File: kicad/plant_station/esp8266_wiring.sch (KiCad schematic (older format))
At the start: 20 parts, among them J1 Conn_02x08_Odd_Even, J17 GPIO, J8 UART, Q4 DMG2301L, U4 ESP-WROOM-02, U5 TPL5110

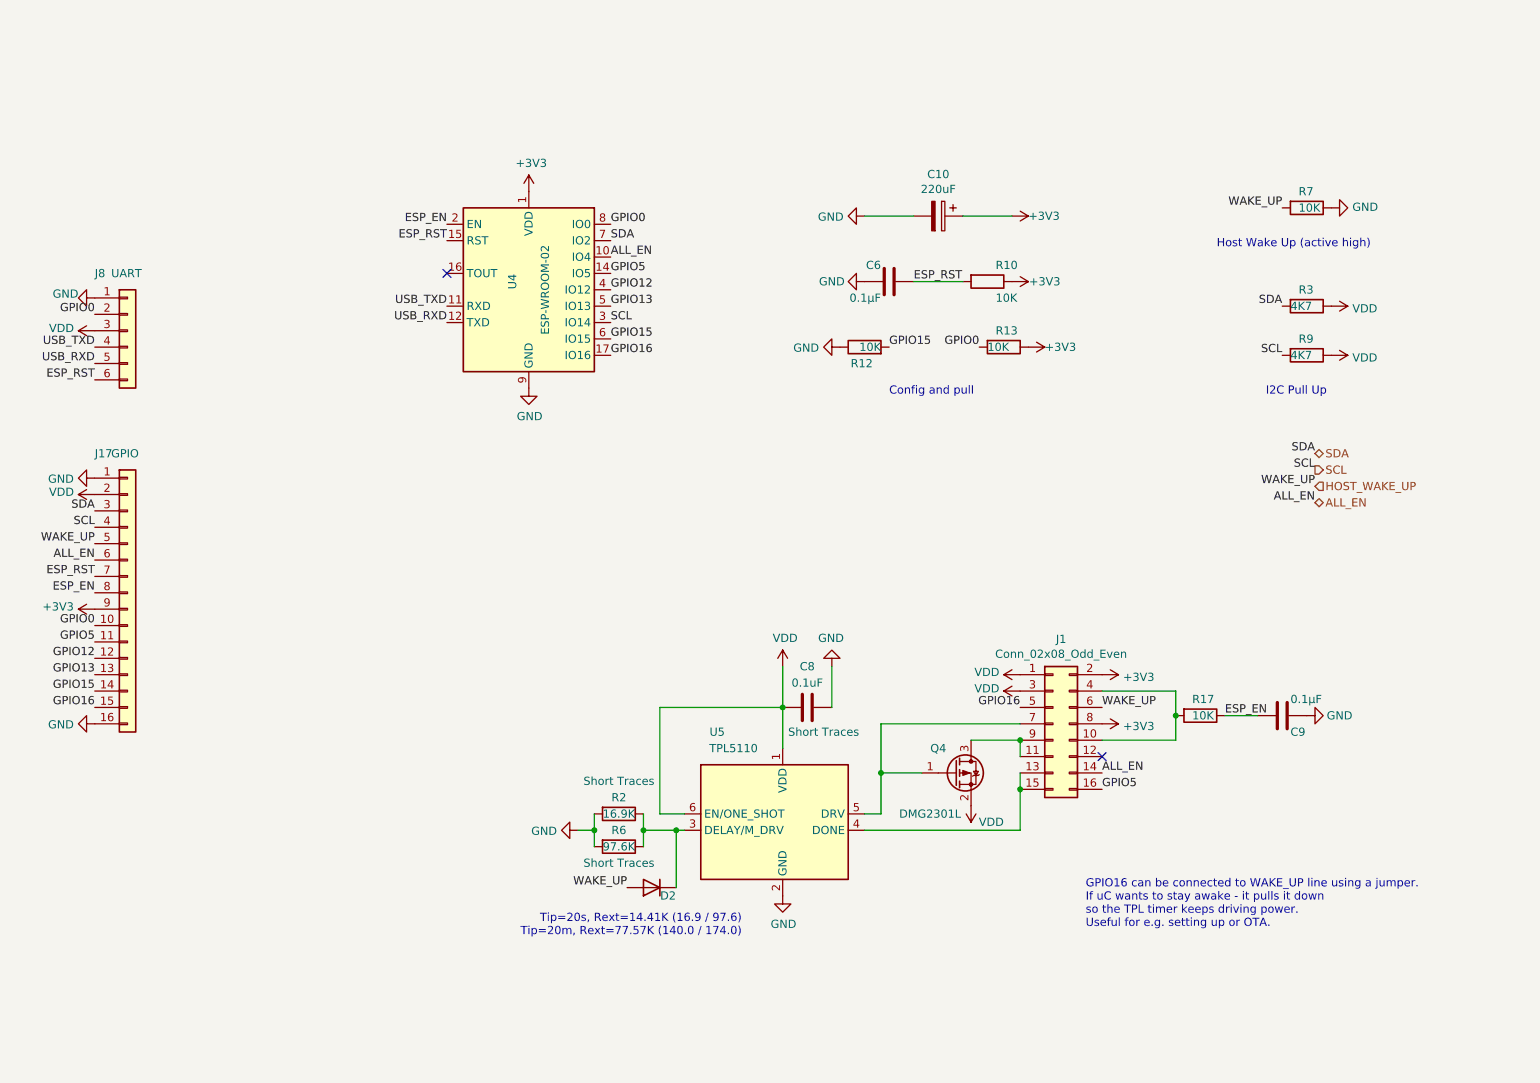
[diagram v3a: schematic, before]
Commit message: Initial board layout complete
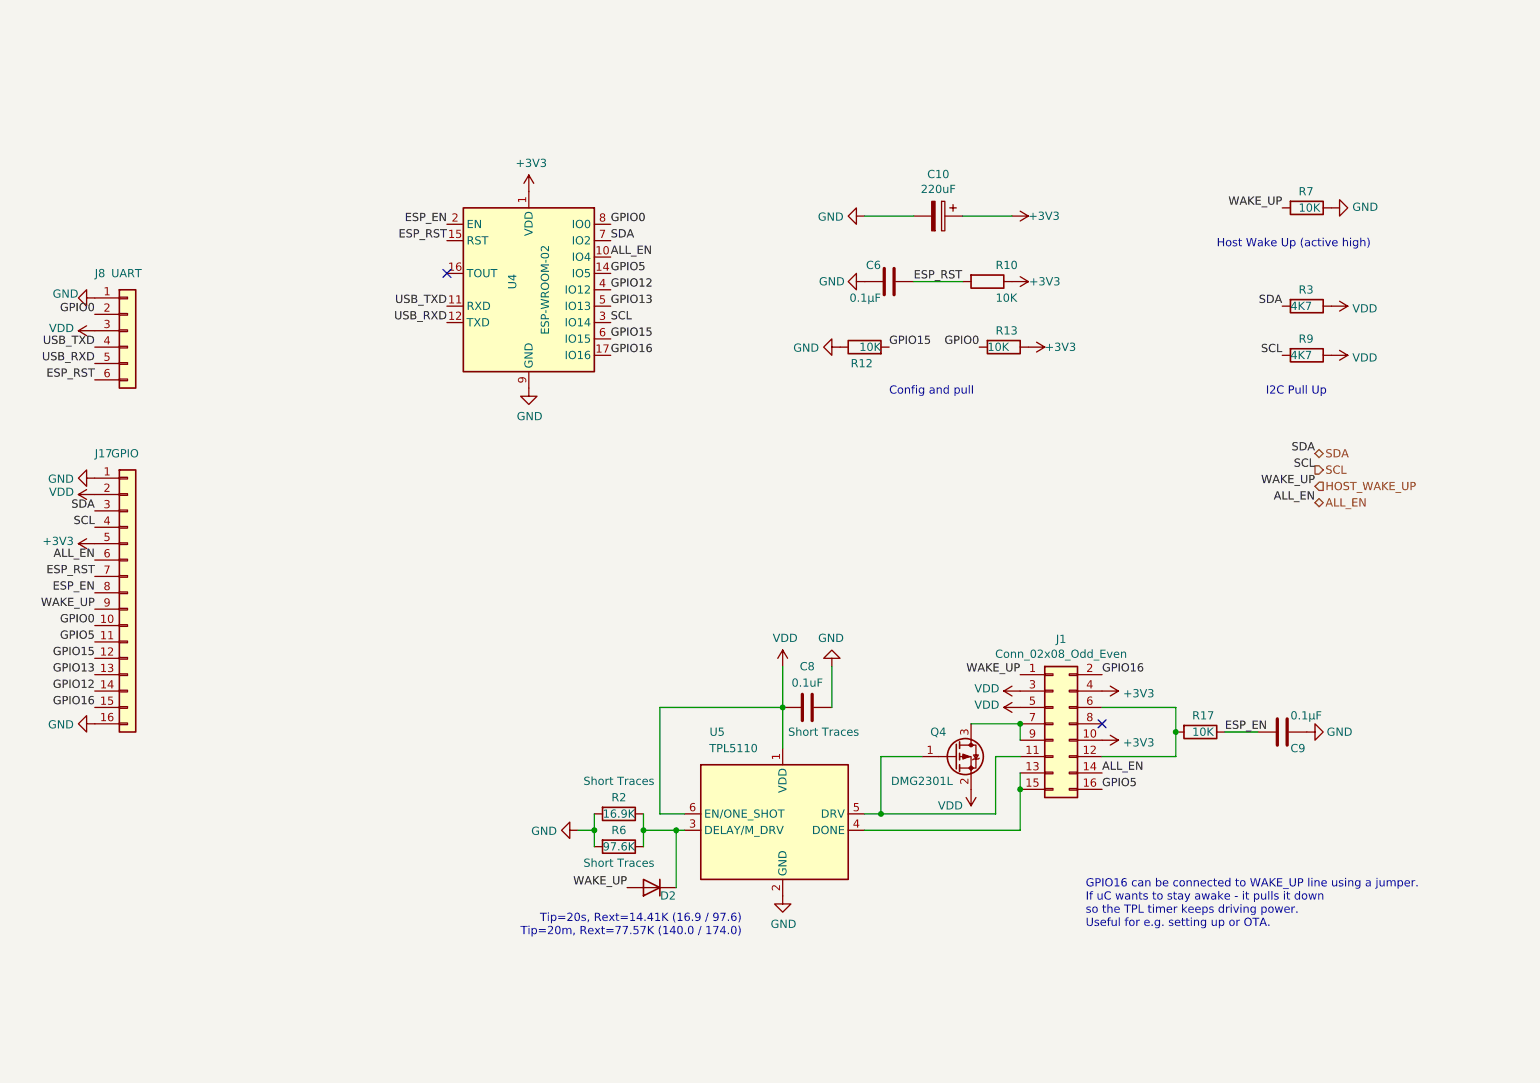
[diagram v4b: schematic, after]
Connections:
- net +3V3: now also J1.10 (Pin_10), J1.4 (Pin_4), J17.5 (Pin_5); no longer J1.2 (Pin_2), J1.8 (Pin_8), J17.9 (Pin_9)
- net GPIO12: now also J17.14 (Pin_14); no longer J17.12 (Pin_12)
- net GPIO15: now also J17.12 (Pin_12); no longer J17.14 (Pin_14)
- net GPIO16: now also J1.2 (Pin_2); no longer J1.5 (Pin_5)
- net HOST_WAKE_UP: now also J1.1 (Pin_1), J17.9 (Pin_9); no longer J1.6 (Pin_6), J17.5 (Pin_5)
- net VDD: now also J1.5 (Pin_5); no longer J1.1 (Pin_1)
- net at Q4.1 (G), U5.5 (DRV): now also J1.11 (Pin_11); no longer J1.7 (Pin_7)
- net at J1.9 (Pin_9), Q4.3 (D): now also J1.7 (Pin_7); no longer J1.11 (Pin_11)
- net at J1.12 (Pin_12): now also J1.6 (Pin_6), R17.2
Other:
- moved on the sheet: C9, Q4, R17
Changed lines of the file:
@@
 	0    1    1    0
 $EndComp
-Text Label 9150 1650 2    50   ~ 0
-WAKE_UP
 Text Notes 8750 1900 0    50   ~ 0
 Host Wake Up (active high)
@@
 	1    0    0    -1
 $EndComp
-Text Label 8050 4700 0    50   ~ 0
+Text Label 7550 4500 2    50   ~ 0
 WAKE_UP
 Text Notes 7950 6050 0    50   ~ 0
@@
 L power:VDD #PWR039
 U 1 1 5F99A85E
-P 7250 5300
-F 0 "#PWR039" H 7250 5150 50  0001 C CNN
-F 1 "VDD" H 7050 5400 50  0000 L CNN
-F 2 "" H 7250 5300 50  0001 C CNN
-F 3 "" H 7250 5300 50  0001 C CNN
-	1    7250 5300
+P 7250 5200
+F 0 "#PWR039" H 7250 5050 50  0001 C CNN
+F 1 "VDD" H 7300 5300 50  0000 L CNN
+F 2 "" H 7250 5200 50  0001 C CNN
+F 3 "" H 7250 5200 50  0001 C CNN
+	1    7250 5200
 	-1   0    0    1
 $EndComp
@@
 L Transistor_FET:DMG2301L Q4
 U 1 1 5F96E6B6
-P 7150 5100
-F 0 "Q4" H 7050 5250 50  0000 C CNN
-F 1 "DMG2301L" H 7000 4850 50  0000 C CNN
-F 2 "Package_TO_SOT_SMD:SOT-23" H 7350 5025 50  0001 L CIN
-F 3 "https://www.diodes.com/assets/Datasheets/DMG2301L.pdf" H 7150 5100 50  0001 L CNN
-	1    7150 5100
-	1    0    0    -1
-$EndComp
-Wire Wire Line
-	6950 5100 6700 5100
-Wire Wire Line
-	6700 5100 6700 5350
+P 7150 5000
+F 0 "Q4" H 7050 5150 50  0000 C CNN
+F 1 "DMG2301L" H 6950 4850 50  0000 C CNN
+F 2 "Package_TO_SOT_SMD:SOT-23" H 7350 4925 50  0001 L CIN
+F 3 "https://www.diodes.com/assets/Datasheets/DMG2301L.pdf" H 7150 5000 50  0001 L CNN
+	1    7150 5000
+	1    0    0    -1
+$EndComp
 Wire Wire Line
 	4950 5450 4850 5450
-Wire Wire Line
-	6700 5100 6700 4800
-Connection ~ 6700 5100
 $Comp
 L power:VDD #PWR033
@@
 Text Label 1900 4300 2    50   ~ 0
 GPIO5
-Text Label 1900 4400 2    50   ~ 0
+Text Label 1900 4600 2    50   ~ 0
 GPIO12
 Text Label 1900 4500 2    50   ~ 0
 GPIO13
-Text Label 1900 4600 2    50   ~ 0
+Text Label 1900 4400 2    50   ~ 0
 GPIO15
-Text Label 1900 3700 2    50   ~ 0
-WAKE_UP
 Text Label 1900 3500 2    50   ~ 0
 SDA
@@
 Text Label 1900 3800 2    50   ~ 0
 ALL_EN
-$Comp
-L power:+3V3 #PWR0104
-U 1 1 5FAF7387
-P 1900 4100
-F 0 "#PWR0104" H 1900 3950 50  0001 C CNN
-F 1 "+3V3" V 1915 4228 50  0000 L CNN
-F 2 "" H 1900 4100 50  0001 C CNN
-F 3 "" H 1900 4100 50  0001 C CNN
-	1    1900 4100
-	0    -1   -1   0
-$EndComp
 Wire Wire Line
 	6700 5350 6600 5350
@@
 $EndComp
 Wire Wire Line
-	9000 4750 8800 4750
-Wire Wire Line
-	8500 4750 8500 4900
-Connection ~ 8500 4750
-Wire Wire Line
-	8050 4900 8500 4900
-Wire Wire Line
-	8500 4600 8500 4750
-Wire Wire Line
-	8050 4600 8500 4600
-NoConn ~ 8050 5000
-Wire Wire Line
-	6700 4800 7550 4800
+	9000 4850 8800 4850
+Wire Wire Line
+	8050 5000 8500 5000
+Wire Wire Line
+	8050 4700 8500 4700
 Wire Wire Line
 	6600 5450 7550 5450
-Wire Wire Line
-	7250 4900 7550 4900
 $Comp
 L power:VDD #PWR040
 U 1 1 5F88FAB9
-P 7550 4500
-F 0 "#PWR040" H 7550 4350 50  0001 C CNN
-F 1 "VDD" V 7565 4627 50  0000 L CNN
-F 2 "" H 7550 4500 50  0001 C CNN
-F 3 "" H 7550 4500 50  0001 C CNN
-	1    7550 4500
-	0    -1   -1   0
-$EndComp
-$Comp
-L power:VDD #PWR041
-U 1 1 5F89065C
 P 7550 4600
-F 0 "#PWR041" H 7550 4450 50  0001 C CNN
+F 0 "#PWR040" H 7550 4450 50  0001 C CNN
 F 1 "VDD" V 7565 4727 50  0000 L CNN
 F 2 "" H 7550 4600 50  0001 C CNN
@@
 	0    -1   -1   0
 $EndComp
-Text Label 8800 4750 0    50   ~ 0
+$Comp
+L power:VDD #PWR041
+U 1 1 5F89065C
+P 7550 4700
+F 0 "#PWR041" H 7550 4550 50  0001 C CNN
+F 1 "VDD" V 7565 4827 50  0000 L CNN
+F 2 "" H 7550 4700 50  0001 C CNN
+F 3 "" H 7550 4700 50  0001 C CNN
+	1    7550 4700
+	0    -1   -1   0
+$EndComp
+Text Label 8800 4850 0    50   ~ 0
 ESP_EN
 $Comp
 L power:+3V3 #PWR043
 U 1 1 5F863AFE
-P 8050 4800
-F 0 "#PWR043" H 8050 4650 50  0001 C CNN
-F 1 "+3V3" V 8065 4928 50  0000 L CNN
-F 2 "" H 8050 4800 50  0001 C CNN
-F 3 "" H 8050 4800 50  0001 C CNN
-	1    8050 4800
+P 8050 4900
+F 0 "#PWR043" H 8050 4750 50  0001 C CNN
+F 1 "+3V3" V 8065 5028 50  0000 L CNN
+F 2 "" H 8050 4900 50  0001 C CNN
+F 3 "" H 8050 4900 50  0001 C CNN
+	1    8050 4900
 	0    1    1    0
 $EndComp
@@
 L power:+3V3 #PWR042
 U 1 1 5F7D8743
-P 8050 4500
-F 0 "#PWR042" H 8050 4350 50  0001 C CNN
-F 1 "+3V3" V 8065 4628 50  0000 L CNN
-F 2 "" H 8050 4500 50  0001 C CNN
-F 3 "" H 8050 4500 50  0001 C CNN
-	1    8050 4500
+P 8050 4600
+F 0 "#PWR042" H 8050 4450 50  0001 C CNN
+F 1 "+3V3" V 8065 4728 50  0000 L CNN
+F 2 "" H 8050 4600 50  0001 C CNN
+F 3 "" H 8050 4600 50  0001 C CNN
+	1    8050 4600
 	0    1    1    0
 $EndComp
@@
 L Device:R R17
 U 1 1 5F58F54F
-P 8650 4750
-F 0 "R17" V 8550 4700 50  0000 L CNN
-F 1 "10K" V 8650 4700 50  0000 L CNN
-F 2 "Resistor_SMD:R_0805_2012Metric" V 8580 4750 50  0001 C CNN
-F 3 "~" H 8650 4750 50  0001 C CNN
-	1    8650 4750
+P 8650 4850
+F 0 "R17" V 8550 4800 50  0000 L CNN
+F 1 "10K" V 8650 4800 50  0000 L CNN
+F 2 "Resistor_SMD:R_0805_2012Metric" V 8580 4850 50  0001 C CNN
+F 3 "~" H 8650 4850 50  0001 C CNN
+	1    8650 4850
 	0    1    1    0
 $EndComp
@@
 L Device:C Cdec?
 U 1 1 5F5944DB
-P 9150 4750
+P 9150 4850
 AR Path="/60DE59F5/5F5944DB" Ref="Cdec?"  Part="1"
 AR Path="/5F5944DB" Ref="Cdec?"  Part="1"
 AR Path="/5F564838/5F5944DB" Ref="C9"  Part="1"
-F 0 "C9" V 9250 4800 50  0000 L CNN
-F 1 "0.1μF" V 9050 4800 50  0000 L CNN
-F 2 "Capacitor_SMD:C_1206_3216Metric" H 9188 4600 50  0001 C CNN
-F 3 "~" H 9150 4750 50  0001 C CNN
-	1    9150 4750
+F 0 "C9" V 9250 4900 50  0000 L CNN
+F 1 "0.1μF" V 9050 4900 50  0000 L CNN
+F 2 "Capacitor_SMD:C_1206_3216Metric" H 9188 4700 50  0001 C CNN
+F 3 "~" H 9150 4850 50  0001 C CNN
+	1    9150 4850
 	0    1    1    0
 $EndComp
@@
 L power:GND #PWR?
 U 1 1 5F59F761
-P 9300 4750
+P 9300 4850
 AR Path="/60DE59F5/5F59F761" Ref="#PWR?"  Part="1"
 AR Path="/5F59F761" Ref="#PWR?"  Part="1"
 AR Path="/5F564838/5F59F761" Ref="#PWR0147"  Part="1"
-F 0 "#PWR0147" H 9300 4500 50  0001 C CNN
-F 1 "GND" V 9300 4550 50  0000 C CNN
-F 2 "" H 9300 4750 50  0001 C CNN
-F 3 "" H 9300 4750 50  0001 C CNN
-	1    9300 4750
-	0    -1   -1   0
-$EndComp
-Wire Wire Line
-	7550 4900 7550 5000
+F 0 "#PWR0147" H 9300 4600 50  0001 C CNN
+F 1 "GND" V 9300 4650 50  0000 C CNN
+F 2 "" H 9300 4850 50  0001 C CNN
+F 3 "" H 9300 4850 50  0001 C CNN
+	1    9300 4850
+	0    -1   -1   0
+$EndComp
 Wire Wire Line
 	7550 5200 7550 5450
-Connection ~ 7550 4900
 Wire Wire Line
 	7550 5100 7550 5200
@@
 Text Label 5050 2550 0    50   ~ 0
 GPIO16
-Text Label 7550 4700 2    50   ~ 0
+Text Label 8050 4500 0    50   ~ 0
 GPIO16
 $Comp
@@
 Text Label 9350 3350 2    50   ~ 0
 WAKE_UP
+Text Label 9150 1650 2    50   ~ 0
+WAKE_UP
+NoConn ~ 8050 4800
+Wire Wire Line
+	7250 4800 7550 4800
+Wire Wire Line
+	7550 4900 7550 4800
+Wire Wire Line
+	7550 5000 7400 5000
+Wire Wire Line
+	7400 5000 7400 5350
+Wire Wire Line
+	7400 5350 6700 5350
+Connection ~ 6700 5350
+Connection ~ 7550 4800
+Wire Wire Line
+	6950 5000 6700 5000
+Wire Wire Line
+	6700 5000 6700 5350
+Connection ~ 8500 4850
+Wire Wire Line
+	8500 4850 8500 5000
+Wire Wire Line
+	8500 4700 8500 4850
+Text Label 1900 4100 2    50   ~ 0
+WAKE_UP
+$Comp
+L power:+3V3 #PWR0104
+U 1 1 5FAF7387
+P 1900 3700
+F 0 "#PWR0104" H 1900 3550 50  0001 C CNN
+F 1 "+3V3" V 1915 3828 50  0000 L CNN
+F 2 "" H 1900 3700 50  0001 C CNN
+F 3 "" H 1900 3700 50  0001 C CNN
+	1    1900 3700
+	0    -1   -1   0
+$EndComp
 $EndSCHEMATC
